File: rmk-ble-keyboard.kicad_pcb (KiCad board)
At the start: 2 copper layers, 301.2 x 94.1 mm, 0 parts

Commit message: add rmk-ble-keyboard %65
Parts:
- added BAT_SW1: MSK-12C02, Button_Switch_SMD:SW_SPDT_PCM12, F.Cu at (77.0, 99.8)
- added C1: 1uf, Capacitor_SMD:C_0603_1608Metric_Pad1.08x0.95mm_HandSolder, B.Cu at (190.0, 135.6)
- added C2: 1uf, Capacitor_SMD:C_0603_1608Metric_Pad1.08x0.95mm_HandSolder, B.Cu at (200.3, 133.7)
- added C3: 10uf, Capacitor_SMD:C_0603_1608Metric_Pad1.08x0.95mm_HandSolder, B.Cu at (197.6, 141.0)
- added C4: 10uf, Capacitor_SMD:C_0603_1608Metric_Pad1.08x0.95mm_HandSolder, B.Cu at (193.5, 141.0)
- added C5: 100nf, Capacitor_SMD:C_0603_1608Metric_Pad1.08x0.95mm_HandSolder, B.Cu at (142.9, 147.6)
- added D1: 1N4148W, Diode_SMD:D_SOD-123, B.Cu at (60.2, 64.4)
- added D10: 1N4148W, Diode_SMD:D_SOD-123, B.Cu at (231.7, 64.4)
- added D11: 1N4148W, Diode_SMD:D_SOD-123, B.Cu at (250.7, 64.4)
- added D12: 1N4148W, Diode_SMD:D_SOD-123, B.Cu at (269.8, 64.4)
- added D13: 1N4148W, Diode_SMD:D_SOD-123, B.Cu at (288.8, 64.4)
- added D14: 1N4148W, Diode_SMD:D_SOD-123, B.Cu at (317.4, 64.4)
- added D15: 1N4148W, Diode_SMD:D_SOD-123, B.Cu at (346.0, 64.4)
- added D16: 1N4148W, Diode_SMD:D_SOD-123, B.Cu at (65.0, 83.4)
- added D17: 1N4148W, Diode_SMD:D_SOD-123, B.Cu at (88.8, 83.4)
- added D18: 1N4148W, Diode_SMD:D_SOD-123, B.Cu at (107.8, 83.4)
- added D19: 1N4148W, Diode_SMD:D_SOD-123, B.Cu at (126.9, 83.4)
- added D2: 1N4148W, Diode_SMD:D_SOD-123, B.Cu at (79.3, 64.4)
- added D20: 1N4148W, Diode_SMD:D_SOD-123, B.Cu at (145.9, 83.4)
- added D21: 1N4148W, Diode_SMD:D_SOD-123, B.Cu at (165.0, 83.4)
- added D22: 1N4148W, Diode_SMD:D_SOD-123, B.Cu at (184.0, 83.4)
- added D23: 1N4148W, Diode_SMD:D_SOD-123, B.Cu at (203.1, 83.4)
- added D24: 1N4148W, Diode_SMD:D_SOD-123, B.Cu at (222.1, 83.4)
- added D25: 1N4148W, Diode_SMD:D_SOD-123, B.Cu at (241.2, 83.4)
- added D26: 1N4148W, Diode_SMD:D_SOD-123, B.Cu at (260.2, 83.4)
- added D27: 1N4148W, Diode_SMD:D_SOD-123, B.Cu at (279.3, 83.4)
- added D28: 1N4148W, Diode_SMD:D_SOD-123, B.Cu at (298.3, 83.4)
- added D29: 1N4148W, Diode_SMD:D_SOD-123, B.Cu at (322.2, 83.4)
- added D3: 1N4148W, Diode_SMD:D_SOD-123, B.Cu at (98.3, 64.4)
- added D30: 1N4148W, Diode_SMD:D_SOD-123, B.Cu at (346.0, 83.4)
- added D31: 1N4148W, Diode_SMD:D_SOD-123, B.Cu at (67.4, 102.5)
- added D32: 1N4148W, Diode_SMD:D_SOD-123, B.Cu at (93.6, 102.5)
- added D33: 1N4148W, Diode_SMD:D_SOD-123, B.Cu at (112.6, 102.5)
- added D34: 1N4148W, Diode_SMD:D_SOD-123, B.Cu at (131.7, 102.5)
- added D35: 1N4148W, Diode_SMD:D_SOD-123, B.Cu at (150.7, 102.5)
- added D36: 1N4148W, Diode_SMD:D_SOD-123, B.Cu at (169.8, 102.5)
- added D37: 1N4148W, Diode_SMD:D_SOD-123, B.Cu at (188.8, 102.5)
- added D38: 1N4148W, Diode_SMD:D_SOD-123, B.Cu at (207.9, 102.5)
- added D39: 1N4148W, Diode_SMD:D_SOD-123, B.Cu at (226.9, 102.5)
- added D4: 1N4148W, Diode_SMD:D_SOD-123, B.Cu at (117.4, 64.4)
- added D40: 1N4148W, Diode_SMD:D_SOD-123, B.Cu at (246.0, 102.5)
- added D41: 1N4148W, Diode_SMD:D_SOD-123, B.Cu at (265.0, 102.5)
- added D42: 1N4148W, Diode_SMD:D_SOD-123, B.Cu at (284.1, 102.5)
- added D43: 1N4148W, Diode_SMD:D_SOD-123, B.Cu at (315.0, 102.5)
- added D44: 1N4148W, Diode_SMD:D_SOD-123, B.Cu at (346.0, 102.5)
- added D45: 1N4148W, Diode_SMD:D_SOD-123, B.Cu at (72.1, 121.5)
- added D46: 1N4148W, Diode_SMD:D_SOD-123, B.Cu at (103.1, 121.5)
- added D47: 1N4148W, Diode_SMD:D_SOD-123, B.Cu at (122.1, 121.5)
- added D48: 1N4148W, Diode_SMD:D_SOD-123, B.Cu at (141.2, 121.5)
- added D49: 1N4148W, Diode_SMD:D_SOD-123, B.Cu at (160.2, 121.5)
- added D5: 1N4148W, Diode_SMD:D_SOD-123, B.Cu at (136.4, 64.4)
- added D50: 1N4148W, Diode_SMD:D_SOD-123, B.Cu at (179.3, 121.5)
- added D51: 1N4148W, Diode_SMD:D_SOD-123, B.Cu at (198.3, 121.5)
- added D52: 1N4148W, Diode_SMD:D_SOD-123, B.Cu at (217.4, 121.5)
- added D53: 1N4148W, Diode_SMD:D_SOD-123, B.Cu at (236.4, 121.5)
- added D54: 1N4148W, Diode_SMD:D_SOD-123, B.Cu at (255.5, 121.5)
- added D55: 1N4148W, Diode_SMD:D_SOD-123, B.Cu at (274.5, 121.5)
- added D56: 1N4148W, Diode_SMD:D_SOD-123, B.Cu at (300.7, 121.5)
- added D57: 1N4148W, Diode_SMD:D_SOD-123, B.Cu at (326.9, 121.5)
- added D58: 1N4148W, Diode_SMD:D_SOD-123, B.Cu at (346.0, 121.5)
- added D59: 1N4148W, Diode_SMD:D_SOD-123, B.Cu at (62.6, 140.6)
- added D6: 1N4148W, Diode_SMD:D_SOD-123, B.Cu at (155.5, 64.4)
- added D60: 1N4148W, Diode_SMD:D_SOD-123, B.Cu at (86.4, 140.6)
- added D61: 1N4148W, Diode_SMD:D_SOD-123, B.Cu at (110.2, 140.6)
- added D62: 1N4148W, Diode_SMD:D_SOD-123, B.Cu at (181.7, 140.6)
- added D63: 1N4148W, Diode_SMD:D_SOD-123, B.Cu at (253.1, 140.6)
- added D64: 1N4148W, Diode_SMD:D_SOD-123, B.Cu at (276.9, 140.6)
- added D65: 1N4148W, Diode_SMD:D_SOD-123, B.Cu at (307.9, 140.6)
- added D66: 1N4148W, Diode_SMD:D_SOD-123, B.Cu at (326.9, 140.6)
- added D67: 1N4148W, Diode_SMD:D_SOD-123, B.Cu at (346.0, 140.6)
- added D68: B5819W, B5819W-SL:SOD-123_L2.7-W1.6-LS3.7-RD-1, B.Cu at (194.6, 137.3)
- added D69: LED, LED_SMD:LED_0603_1608Metric_Pad1.05x0.95mm_HandSolder, F.Cu at (63.7, 108.6)
- added D7: 1N4148W, Diode_SMD:D_SOD-123, B.Cu at (174.5, 64.4)
- added D70: GREEN LED, LED_SMD:LED_0603_1608Metric_Pad1.05x0.95mm_HandSolder, F.Cu at (199.8, 145.5)
- added D8: 1N4148W, Diode_SMD:D_SOD-123, B.Cu at (193.6, 64.4)
- added D9: 1N4148W, Diode_SMD:D_SOD-123, B.Cu at (212.6, 64.4)
- added J1: ~, XY-MX1.25-2A71:CONN-SMD_2P-P1.25_XYECONN_XY-MX1.25-2A71, B.Cu at (76.3, 91.5)
- added J2: JST_SH_SM04B-SRSS-TB, Connector_JST:JST_SH_SM04B-SRSS-TB_1x04-1MP_P1.00mm_Horizontal, B.Cu at (104.6, 71.4)
- added J4: Debug, Connector_PinHeader_2.54mm:PinHeader_1x04_P2.54mm_Vertical, B.Cu at (51.4, 98.5)
- added J5: RGB, Connector_PinHeader_1.27mm:PinHeader_1x03_P1.27mm_Vertical, B.Cu at (146.2, 147.6)
- added Q1: Si2301CDS, Package_TO_SOT_SMD:SOT-23, B.Cu at (197.5, 137.3)
- added R1: 806K, Resistor_SMD:R_0603_1608Metric_Pad0.98x0.95mm_HandSolder, B.Cu at (70.6, 92.2)
- added R10: 10K, Resistor_SMD:R_0603_1608Metric_Pad0.98x0.95mm_HandSolder, F.Cu at (199.8, 144.0)
- added R2: 10K, Resistor_SMD:R_0603_1608Metric_Pad0.98x0.95mm_HandSolder, F.Cu at (72.8, 96.7)
- added R3: 2M, Resistor_SMD:R_0603_1608Metric_Pad0.98x0.95mm_HandSolder, B.Cu at (70.6, 90.7)
- added R6: 3K, Resistor_SMD:R_0603_1608Metric_Pad0.98x0.95mm_HandSolder, B.Cu at (190.0, 145.1)
- added R7: 100K, Resistor_SMD:R_0603_1608Metric_Pad0.98x0.95mm_HandSolder, B.Cu at (190.0, 139.0)
- added R8: 0.4, Resistor_SMD:R_0805_2012Metric_Pad1.20x1.40mm_HandSolder, B.Cu at (190.0, 142.6)
- added R9: 1K, Resistor_SMD:R_0603_1608Metric_Pad0.98x0.95mm_HandSolder, F.Cu at (63.7, 107.0)
- added REF**: Stabilizer_Cherry_MX_2.00u, PCM_Mounting_Keyboard_Stabilizer:Stabilizer_Cherry_MX_2.00u, F.Cu at (314.3, 64.4)
- added REF**: Stabilizer_Cherry_MX_6.25u, PCM_Mounting_Keyboard_Stabilizer:Stabilizer_Cherry_MX_6.25u, F.Cu at (178.6, 140.6)
- added REF**: Stabilizer_Cherry_MX_2.00u, PCM_Mounting_Keyboard_Stabilizer:Stabilizer_Cherry_MX_2.00u, F.Cu at (311.9, 102.5)
- added REF**: Stabilizer_Cherry_MX_2.00u, PCM_Mounting_Keyboard_Stabilizer:Stabilizer_Cherry_MX_2.00u, F.Cu at (69.0, 121.5)
- added SW1: esc, PCM_Switch_Keyboard_Hotswap_Kailh:SW_Hotswap_Kailh_MX_Plated_1.00u, F.Cu at (57.1, 64.4)
- added SW10: 9, PCM_Switch_Keyboard_Hotswap_Kailh:SW_Hotswap_Kailh_MX_Plated_1.00u, F.Cu at (228.6, 64.4)
- added SW11: 0, PCM_Switch_Keyboard_Hotswap_Kailh:SW_Hotswap_Kailh_MX_Plated_1.00u, F.Cu at (247.6, 64.4)
- added SW12: -, PCM_Switch_Keyboard_Hotswap_Kailh:SW_Hotswap_Kailh_MX_Plated_1.00u, F.Cu at (266.7, 64.4)
- added SW13: =, PCM_Switch_Keyboard_Hotswap_Kailh:SW_Hotswap_Kailh_MX_Plated_1.00u, F.Cu at (285.7, 64.4)
- added SW14: backspace, PCM_Switch_Keyboard_Hotswap_Kailh:SW_Hotswap_Kailh_MX_Plated_2.00u, F.Cu at (314.3, 64.4)
- added SW15: del, PCM_Switch_Keyboard_Hotswap_Kailh:SW_Hotswap_Kailh_MX_Plated_1.00u, F.Cu at (342.9, 64.4)
- added SW16: tab, PCM_Switch_Keyboard_Hotswap_Kailh:SW_Hotswap_Kailh_MX_Plated_1.50u, F.Cu at (61.9, 83.4)
- added SW17: q, PCM_Switch_Keyboard_Hotswap_Kailh:SW_Hotswap_Kailh_MX_Plated_1.00u, F.Cu at (85.7, 83.4)
- added SW18: w, PCM_Switch_Keyboard_Hotswap_Kailh:SW_Hotswap_Kailh_MX_Plated_1.00u, F.Cu at (104.7, 83.4)
- added SW19: e, PCM_Switch_Keyboard_Hotswap_Kailh:SW_Hotswap_Kailh_MX_Plated_1.00u, F.Cu at (123.8, 83.4)
- added SW2: 1, PCM_Switch_Keyboard_Hotswap_Kailh:SW_Hotswap_Kailh_MX_Plated_1.00u, F.Cu at (76.2, 64.4)
- added SW20: r, PCM_Switch_Keyboard_Hotswap_Kailh:SW_Hotswap_Kailh_MX_Plated_1.00u, F.Cu at (142.8, 83.4)
- added SW21: t, PCM_Switch_Keyboard_Hotswap_Kailh:SW_Hotswap_Kailh_MX_Plated_1.00u, F.Cu at (161.9, 83.4)
- added SW22: y, PCM_Switch_Keyboard_Hotswap_Kailh:SW_Hotswap_Kailh_MX_Plated_1.00u, F.Cu at (180.9, 83.4)
- added SW23: u, PCM_Switch_Keyboard_Hotswap_Kailh:SW_Hotswap_Kailh_MX_Plated_1.00u, F.Cu at (200.0, 83.4)
- added SW24: i, PCM_Switch_Keyboard_Hotswap_Kailh:SW_Hotswap_Kailh_MX_Plated_1.00u, F.Cu at (219.0, 83.4)
- added SW25: o, PCM_Switch_Keyboard_Hotswap_Kailh:SW_Hotswap_Kailh_MX_Plated_1.00u, F.Cu at (238.1, 83.4)
- added SW26: p, PCM_Switch_Keyboard_Hotswap_Kailh:SW_Hotswap_Kailh_MX_Plated_1.00u, F.Cu at (257.1, 83.4)
- added SW27: [, PCM_Switch_Keyboard_Hotswap_Kailh:SW_Hotswap_Kailh_MX_Plated_1.00u, F.Cu at (276.2, 83.4)
- added SW28: ], PCM_Switch_Keyboard_Hotswap_Kailh:SW_Hotswap_Kailh_MX_Plated_1.00u, F.Cu at (295.2, 83.4)
- added SW29: \, PCM_Switch_Keyboard_Hotswap_Kailh:SW_Hotswap_Kailh_MX_Plated_1.50u, F.Cu at (319.1, 83.4)
- added SW3: 2, PCM_Switch_Keyboard_Hotswap_Kailh:SW_Hotswap_Kailh_MX_Plated_1.00u, F.Cu at (95.2, 64.4)
- added SW30: pgup, PCM_Switch_Keyboard_Hotswap_Kailh:SW_Hotswap_Kailh_MX_Plated_1.00u, F.Cu at (342.9, 83.4)
- added SW31: capslock, PCM_Switch_Keyboard_Hotswap_Kailh:SW_Hotswap_Kailh_MX_Plated_1.75u, F.Cu at (64.3, 102.5)
- added SW32: a, PCM_Switch_Keyboard_Hotswap_Kailh:SW_Hotswap_Kailh_MX_Plated_1.00u, F.Cu at (90.5, 102.5)
- added SW33: s, PCM_Switch_Keyboard_Hotswap_Kailh:SW_Hotswap_Kailh_MX_Plated_1.00u, F.Cu at (109.5, 102.5)
- added SW34: d, PCM_Switch_Keyboard_Hotswap_Kailh:SW_Hotswap_Kailh_MX_Plated_1.00u, F.Cu at (128.6, 102.5)
- added SW35: f, PCM_Switch_Keyboard_Hotswap_Kailh:SW_Hotswap_Kailh_MX_Plated_1.00u, F.Cu at (147.6, 102.5)
- added SW36: g, PCM_Switch_Keyboard_Hotswap_Kailh:SW_Hotswap_Kailh_MX_Plated_1.00u, F.Cu at (166.7, 102.5)
- added SW37: h, PCM_Switch_Keyboard_Hotswap_Kailh:SW_Hotswap_Kailh_MX_Plated_1.00u, F.Cu at (185.7, 102.5)
- added SW38: j, PCM_Switch_Keyboard_Hotswap_Kailh:SW_Hotswap_Kailh_MX_Plated_1.00u, F.Cu at (204.8, 102.5)
- added SW39: k, PCM_Switch_Keyboard_Hotswap_Kailh:SW_Hotswap_Kailh_MX_Plated_1.00u, F.Cu at (223.8, 102.5)
- added SW4: 3, PCM_Switch_Keyboard_Hotswap_Kailh:SW_Hotswap_Kailh_MX_Plated_1.00u, F.Cu at (114.3, 64.4)
- added SW40: l, PCM_Switch_Keyboard_Hotswap_Kailh:SW_Hotswap_Kailh_MX_Plated_1.00u, F.Cu at (242.9, 102.5)
- added SW41: ;, PCM_Switch_Keyboard_Hotswap_Kailh:SW_Hotswap_Kailh_MX_Plated_1.00u, F.Cu at (261.9, 102.5)
- added SW42: ', PCM_Switch_Keyboard_Hotswap_Kailh:SW_Hotswap_Kailh_MX_Plated_1.00u, F.Cu at (281.0, 102.5)
- added SW43: enter, PCM_Switch_Keyboard_Hotswap_Kailh:SW_Hotswap_Kailh_MX_Plated_2.25u, F.Cu at (311.9, 102.5)
- added SW44: pgdn, PCM_Switch_Keyboard_Hotswap_Kailh:SW_Hotswap_Kailh_MX_Plated_1.00u, F.Cu at (342.9, 102.5)
- added SW45: lshift, PCM_Switch_Keyboard_Hotswap_Kailh:SW_Hotswap_Kailh_MX_Plated_2.25u, F.Cu at (69.0, 121.5)
- added SW46: z, PCM_Switch_Keyboard_Hotswap_Kailh:SW_Hotswap_Kailh_MX_Plated_1.00u, F.Cu at (100.0, 121.5)
- added SW47: x, PCM_Switch_Keyboard_Hotswap_Kailh:SW_Hotswap_Kailh_MX_Plated_1.00u, F.Cu at (119.0, 121.5)
- added SW48: c, PCM_Switch_Keyboard_Hotswap_Kailh:SW_Hotswap_Kailh_MX_Plated_1.00u, F.Cu at (138.1, 121.5)
- added SW49: v, PCM_Switch_Keyboard_Hotswap_Kailh:SW_Hotswap_Kailh_MX_Plated_1.00u, F.Cu at (157.1, 121.5)
- added SW5: 4, PCM_Switch_Keyboard_Hotswap_Kailh:SW_Hotswap_Kailh_MX_Plated_1.00u, F.Cu at (133.3, 64.4)
- added SW50: b, PCM_Switch_Keyboard_Hotswap_Kailh:SW_Hotswap_Kailh_MX_Plated_1.00u, F.Cu at (176.2, 121.5)
- added SW51: n, PCM_Switch_Keyboard_Hotswap_Kailh:SW_Hotswap_Kailh_MX_Plated_1.00u, F.Cu at (195.2, 121.5)
- added SW52: m, PCM_Switch_Keyboard_Hotswap_Kailh:SW_Hotswap_Kailh_MX_Plated_1.00u, F.Cu at (214.3, 121.5)
- added SW53: ,, PCM_Switch_Keyboard_Hotswap_Kailh:SW_Hotswap_Kailh_MX_Plated_1.00u, F.Cu at (233.3, 121.5)
- added SW54: ., PCM_Switch_Keyboard_Hotswap_Kailh:SW_Hotswap_Kailh_MX_Plated_1.00u, F.Cu at (252.4, 121.5)
- added SW55: /, PCM_Switch_Keyboard_Hotswap_Kailh:SW_Hotswap_Kailh_MX_Plated_1.00u, F.Cu at (271.4, 121.5)
- added SW56: rshift, PCM_Switch_Keyboard_Hotswap_Kailh:SW_Hotswap_Kailh_MX_Plated_1.75u, F.Cu at (297.6, 121.5)
- added SW57: up, PCM_Switch_Keyboard_Hotswap_Kailh:SW_Hotswap_Kailh_MX_Plated_1.00u, F.Cu at (323.8, 121.5)
- added SW58: fn, PCM_Switch_Keyboard_Hotswap_Kailh:SW_Hotswap_Kailh_MX_Plated_1.00u, F.Cu at (342.9, 121.5)
- added SW59: lctrl, PCM_Switch_Keyboard_Hotswap_Kailh:SW_Hotswap_Kailh_MX_Plated_1.25u, F.Cu at (59.5, 140.6)
- added SW6: 5, PCM_Switch_Keyboard_Hotswap_Kailh:SW_Hotswap_Kailh_MX_Plated_1.00u, F.Cu at (152.4, 64.4)
- added SW60: lgui, PCM_Switch_Keyboard_Hotswap_Kailh:SW_Hotswap_Kailh_MX_Plated_1.25u, F.Cu at (83.3, 140.6)
- added SW61: lalt, PCM_Switch_Keyboard_Hotswap_Kailh:SW_Hotswap_Kailh_MX_Plated_1.25u, F.Cu at (107.1, 140.6)
- added SW62: space, PCM_Switch_Keyboard_Hotswap_Kailh:SW_Hotswap_Kailh_MX_Plated_6.25u, F.Cu at (178.6, 140.6)
- added SW63: ralt, PCM_Switch_Keyboard_Hotswap_Kailh:SW_Hotswap_Kailh_MX_Plated_1.25u, F.Cu at (250.0, 140.6)
- added SW64: menu, PCM_Switch_Keyboard_Hotswap_Kailh:SW_Hotswap_Kailh_MX_Plated_1.25u, F.Cu at (273.8, 140.6)
- added SW65: left, PCM_Switch_Keyboard_Hotswap_Kailh:SW_Hotswap_Kailh_MX_Plated_1.00u, F.Cu at (304.8, 140.6)
- added SW66: down, PCM_Switch_Keyboard_Hotswap_Kailh:SW_Hotswap_Kailh_MX_Plated_1.00u, F.Cu at (323.8, 140.6)
- added SW67: right, PCM_Switch_Keyboard_Hotswap_Kailh:SW_Hotswap_Kailh_MX_Plated_1.00u, F.Cu at (342.9, 140.6)
- added SW7: 6, PCM_Switch_Keyboard_Hotswap_Kailh:SW_Hotswap_Kailh_MX_Plated_1.00u, F.Cu at (171.4, 64.4)
- added SW8: 7, PCM_Switch_Keyboard_Hotswap_Kailh:SW_Hotswap_Kailh_MX_Plated_1.00u, F.Cu at (190.5, 64.4)
- added SW9: 8, PCM_Switch_Keyboard_Hotswap_Kailh:SW_Hotswap_Kailh_MX_Plated_1.00u, F.Cu at (209.5, 64.4)
- added U1: XC6206PxxxMR, Package_TO_SOT_SMD:SOT-23-3, B.Cu at (197.5, 133.6)
- added U2: TP4056, TP4056:ESOP-8_L4.9-W3.9-P1.27-LS6.0-BL-EP, B.Cu at (195.6, 144.5)
- added U4: ~, E73_2G4M08S1C:E73(2G4M08S1C), B.Cu at (205.9, 132.9)
- added Y1: 32.768KHZ, Crystal:Crystal_SMD_3215-2Pin_3.2x1.5mm, B.Cu at (202.6, 143.2)
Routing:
- net /matrix/row1: track 0.00 -> 392.7 mm, vias 0 -> 18
- net /matrix/row2: track 0.00 -> 368.0 mm, vias 0 -> 18
- net /matrix/row5: track 0.00 -> 350.0 mm, vias 0 -> 10
- net /matrix/row3: track 0.00 -> 345.8 mm, vias 0 -> 17
- net /matrix/row4: track 0.00 -> 333.3 mm, vias 0 -> 16
- net /matrix/col1: track 0.00 -> 245.3 mm, vias 0 -> 1
- net /matrix/col2: track 0.00 -> 235.6 mm, vias 0 -> 1
- net VBUS: track 0.00 -> 228.4 mm, vias 0 -> 4
- net /matrix/col3: track 0.00 -> 209.7 mm, vias 0 -> 4
- net /matrix/col15: track 0.00 -> 201.9 mm, vias 0 -> 2
- net 3V3: track 0.00 -> 200.2 mm, vias 0 -> 5
- net /mcu/swd: track 0.00 -> 195.3 mm, vias 0 -> 2
- net /mcu/swc: track 0.00 -> 194.2 mm, vias 0 -> 1
- net /matrix/col14: track 0.00 -> 191.3 mm, vias 0 -> 2
- net /mcu/bat_adc: track 0.00 -> 184.6 mm, vias 0 -> 6
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- added copper zone on B.Cu, net GND
- added copper zone on F.Cu, net GND
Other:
- outline, holes or cut-outs redrawn
- board text added: "+5v rgb gnd"
- board text added: "C1"
- board text added: "C2"
- board text added: "C3"
- board text added: "C4"
- board text added: "Li+"
- board text added: "Li-"
- board text added: "R6"
- board text added: "R7"
- board text added: "R8"
- board text added: "TP4056"
- board text added: "V - + G"
- board text added: "XC6206"
- board text added: "clk"
- board text added: "dio"
- board text added: "gnd"
- board text added: "off"
- board text added: "on"
- board text added: "rmk ble keyboard %65 -- rev 1.0"
- board text added: "vcc"

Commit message: add rmk-ble-keyboard %65
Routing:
- net /matrix/row2: track 368.0 -> 369.6 mm
- net GND: vias 90 -> 94

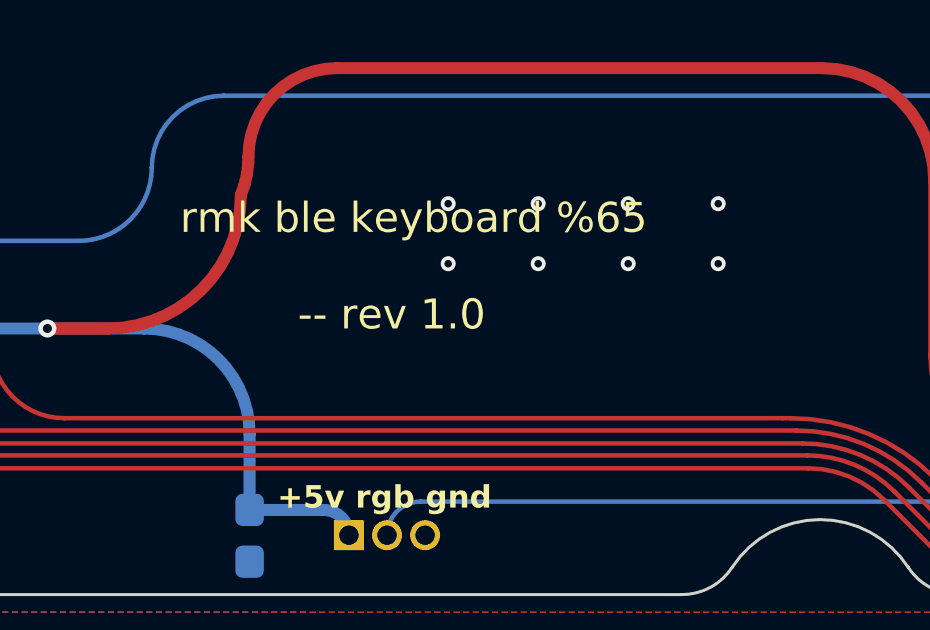
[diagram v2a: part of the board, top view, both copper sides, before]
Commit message: update rmk-ble-keyboard %65
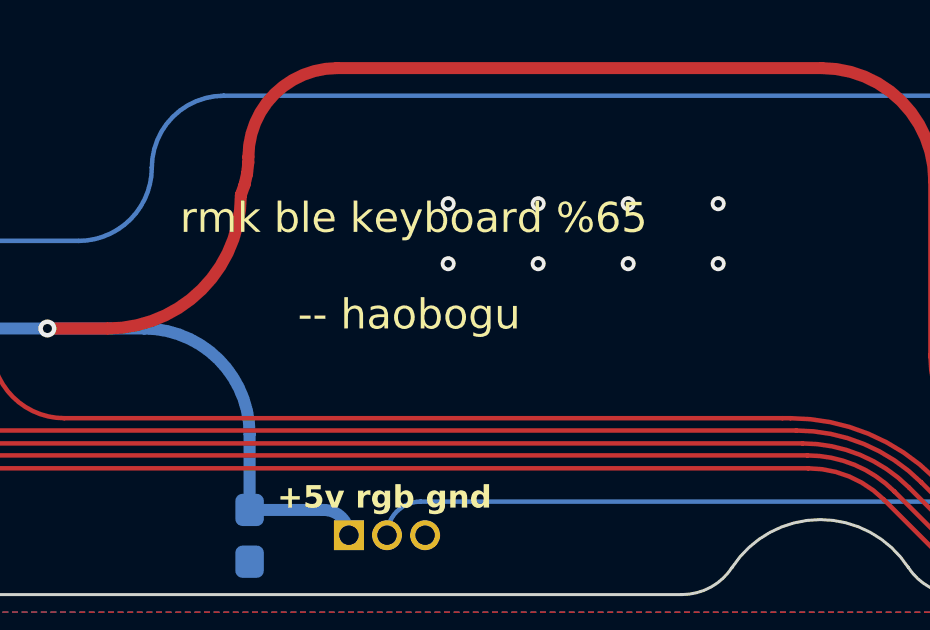
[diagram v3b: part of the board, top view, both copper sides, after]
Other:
- board text added: "rmk ble keyboard %65 -- haobogu"
- board text removed: "rmk ble keyboard %65 -- rev 1.0"
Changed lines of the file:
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@@
 		)
 	)
-	(gr_text "rmk ble keyboard %65\n\n         -- rev 1.0"
+	(gr_text "rmk ble keyboard %65\n\n         -- haobogu"
 		(at 140.56 140.78 0)
 		(layer "F.SilkS")

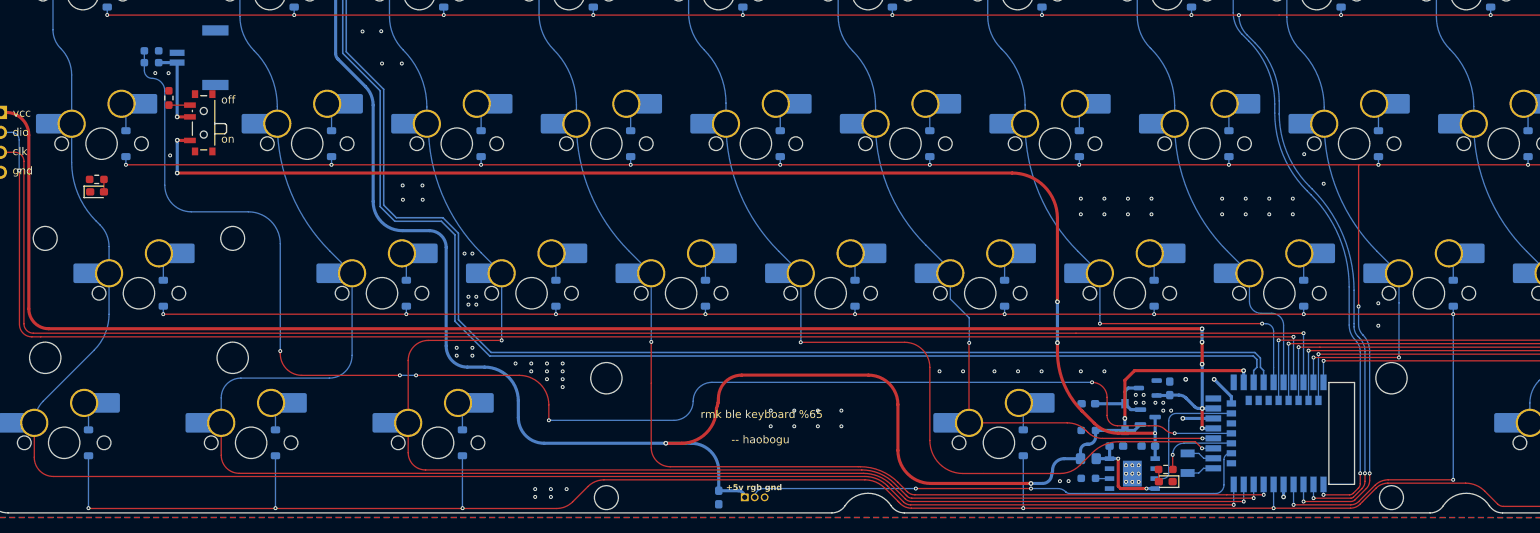
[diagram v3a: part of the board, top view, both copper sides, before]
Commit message: update rmk-ble-keyboard %65
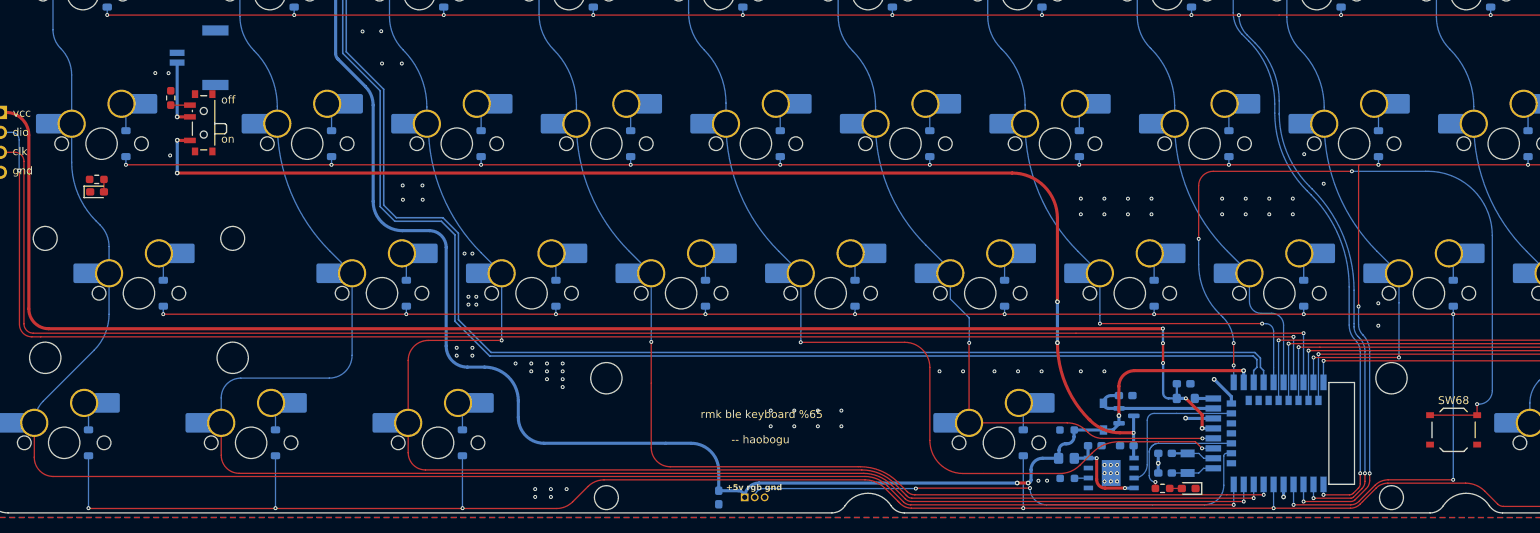
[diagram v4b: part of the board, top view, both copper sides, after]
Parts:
- removed R6: 3K, Resistor_SMD:R_0603_1608Metric_Pad0.98x0.95mm_HandSolder
- removed R7: 100K, Resistor_SMD:R_0603_1608Metric_Pad0.98x0.95mm_HandSolder
- removed R8: 0.4, Resistor_SMD:R_0805_2012Metric_Pad1.20x1.40mm_HandSolder
- removed U2: TP4056, TP4056:ESOP-8_L4.9-W3.9-P1.27-LS6.0-BL-EP
- added C6: 12pf, Capacitor_SMD:C_0603_1608Metric_Pad1.08x0.95mm_HandSolder, B.Cu at (199.7, 144.4)
- added C7: 12pf, Capacitor_SMD:C_0603_1608Metric_Pad1.08x0.95mm_HandSolder, B.Cu at (199.7, 141.9)
- added L1: 10uH, PCM_Inductor_SMD_AKL:L_0805_2012Metric_Pad1.05x1.20mm_HandSolder, B.Cu at (202.4, 134.9)
- added R4: 100K, Resistor_SMD:R_0603_1608Metric_Pad0.98x0.95mm_HandSolder, B.Cu at (187.2, 139.0)
- added SW68: SW_Push, Button_Switch_SMD:SW_Push_1P1T_XKB_TS-1187A, F.Cu at (236.5, 139.0)
- C1, C2: value 1uf -> 4.7uf
- R1: value 806K -> 10K; moved to F.Cu
- R2: value 10K -> 3K; moved to B.Cu
- R3: value 2M -> 0.4; footprint Resistor_SMD:R_0603_1608Metric_Pad0.98x0.95mm_HandSolder -> Resistor_SMD:R_0805_2012Metric_Pad1.20x1.40mm_HandSolder
- U1: value XC6206PxxxMR -> TP4056; footprint Package_TO_SOT_SMD:SOT-23-3 -> TP4056:ESOP-8_L4.9-W3.9-P1.27-LS6.0-BL-EP
- moved R3 127.6 mm to (187.2, 142.6)
- moved R2 124.3 mm to (187.3, 145.1), turned to 0 degrees
- moved C1 12.4 mm to (202.1, 133.1), turned to 0 degrees
- moved U1 11.8 mm to (192.9, 144.4), turned to 90 degrees
- moved C2 5.69 mm to (194.7, 134.6), turned to 0 degrees
- moved R1 5.12 mm to (73.1, 96.7), turned to -90 degrees
- moved D70 3.05 mm to (202.7, 146.4)
- moved C3 2.74 mm to (194.9, 141.0)
- moved C4 2.74 mm to (190.8, 141.0)
- moved D68 2.74 mm to (191.9, 137.3)
- moved Q1 2.72 mm to (194.8, 137.2)
- moved R10 2.45 mm to (199.4, 146.4), turned to 0 degrees
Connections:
- BAT_SW1 pad 1: /power/Li+ -> /mcu/Li+
- C1 pad 1: Net-(D68--) -> 3V3
- C2 pad 1: 3V3 -> VDDH
- C3 pad 1: /power/Li+ -> /mcu/Li+
- C4 pad 1: /power/Vin -> /mcu/Vin
- D68 pad 1: Net-(D68--) -> VDDH
- Q1 pad 2: Net-(D68--) -> VDDH
- Q1 pad 3: /power/Li+ -> /mcu/Li+
- R1 pad 1: Net-(BAT_SW1-B) -> unconnected-(R1-Pad1)
- R1 pad 2: /mcu/bat_adc -> Net-(BAT_SW1-C)
- R2 pad 1: unconnected-(R2-Pad1) -> GND
- R2 pad 2: Net-(BAT_SW1-C) -> Net-(U1-PROG)
- R3 pad 1: /mcu/bat_adc -> VBUS
- R3 pad 2: GND -> /mcu/Vin
- U1 pad 2: 3V3 -> Net-(U1-PROG)
- U1 pad 3: Net-(D68--) -> GND
- U4 pad 18: /mcu/bat_adc -> unconnected-(U4-AI2-Pad18)
- U4 pad 23: 3V3 -> VDDH
- U4 pad 25: unconnected-(U4-DCH-Pad25) -> Net-(U4-DCH)
- U4 pad 26: unconnected-(U4-RST-Pad26) -> Net-(U4-RST)
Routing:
- net /mcu/bat_adc: track 184.6 -> 0.00 mm, vias 6 -> 0
- net /power/Li+: track 161.9 -> 0.00 mm, vias 5 -> 0
- net /mcu/Li+: track 0.00 -> 159.2 mm, vias 0 -> 5
- net Net-(U4-RST): track 0.00 -> 99.0 mm, vias 0 -> 5
- net VBUS: track 228.4 -> 201.8 mm
- net VDDH: track 0.00 -> 16.8 mm
- net /power/Vin: track 12.7 -> 0.00 mm, vias 2 -> 0
- net /mcu/Vin: track 0.00 -> 12.4 mm, vias 0 -> 2
- net Net-(D68--): track 9.59 -> 0.00 mm
- net 3V3: track 200.2 -> 192.5 mm
- net /mcu/charging_led: track 10.1 -> 16.1 mm
- net GND: track 9.48 -> 12.6 mm, vias 94 -> 86
- net Net-(U4-DCH): track 0.00 -> 2.35 mm
- net Net-(BAT_SW1-B): track 10.9 -> 8.55 mm
- net /mcu/CHARGE: track 17.2 -> 19.5 mm
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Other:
- board text removed: "C1"
- board text removed: "C2"
- board text removed: "C3"
- board text removed: "C4"
- board text removed: "R6"
- board text removed: "R7"
- board text removed: "R8"
- board text removed: "TP4056"
- board text removed: "XC6206"
